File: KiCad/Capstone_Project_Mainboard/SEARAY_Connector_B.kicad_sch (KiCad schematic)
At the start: 1 part, among them J1 ASP-134486

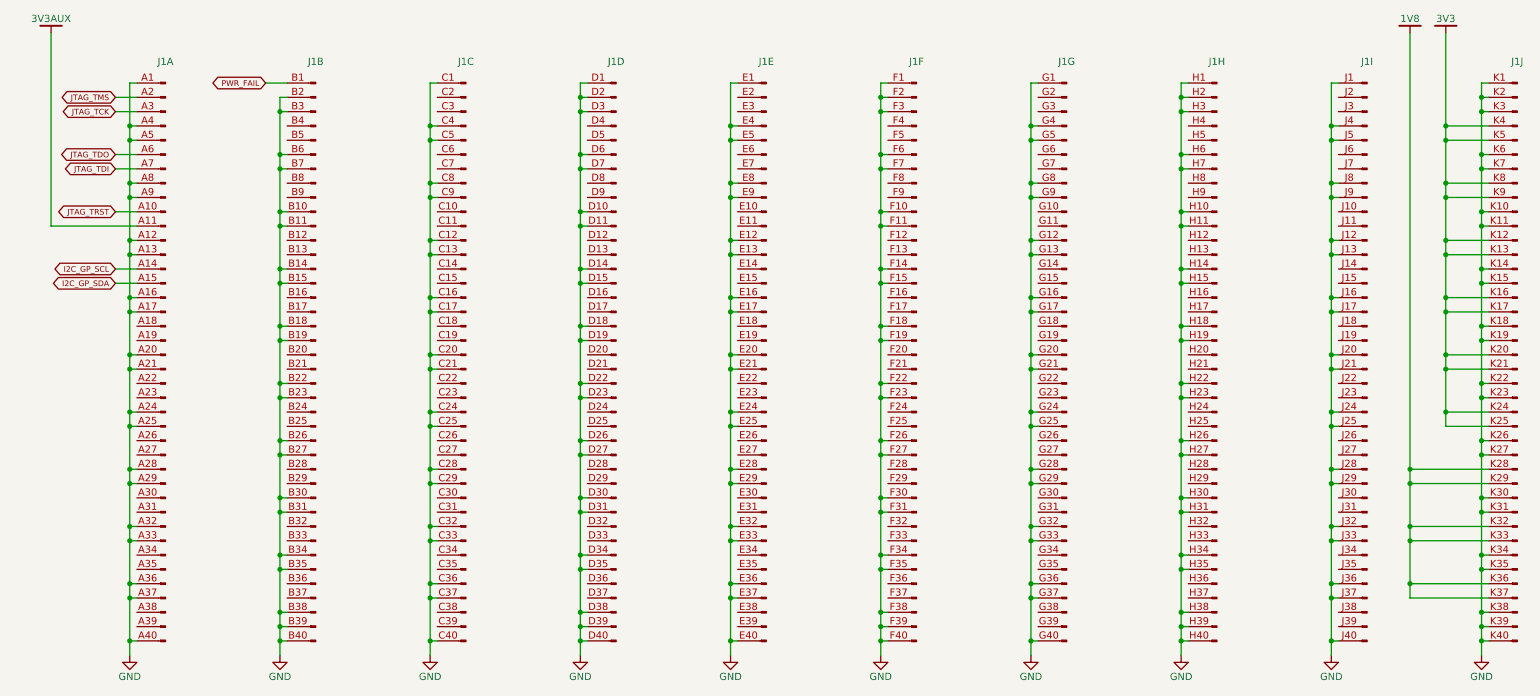
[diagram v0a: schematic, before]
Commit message: Updated FPGA Footprint
Added die-to-pad length offsets to all pins of the FFG676 package. These values were derived from the delay files provided in Vivado.
+ Other minor bugfixes
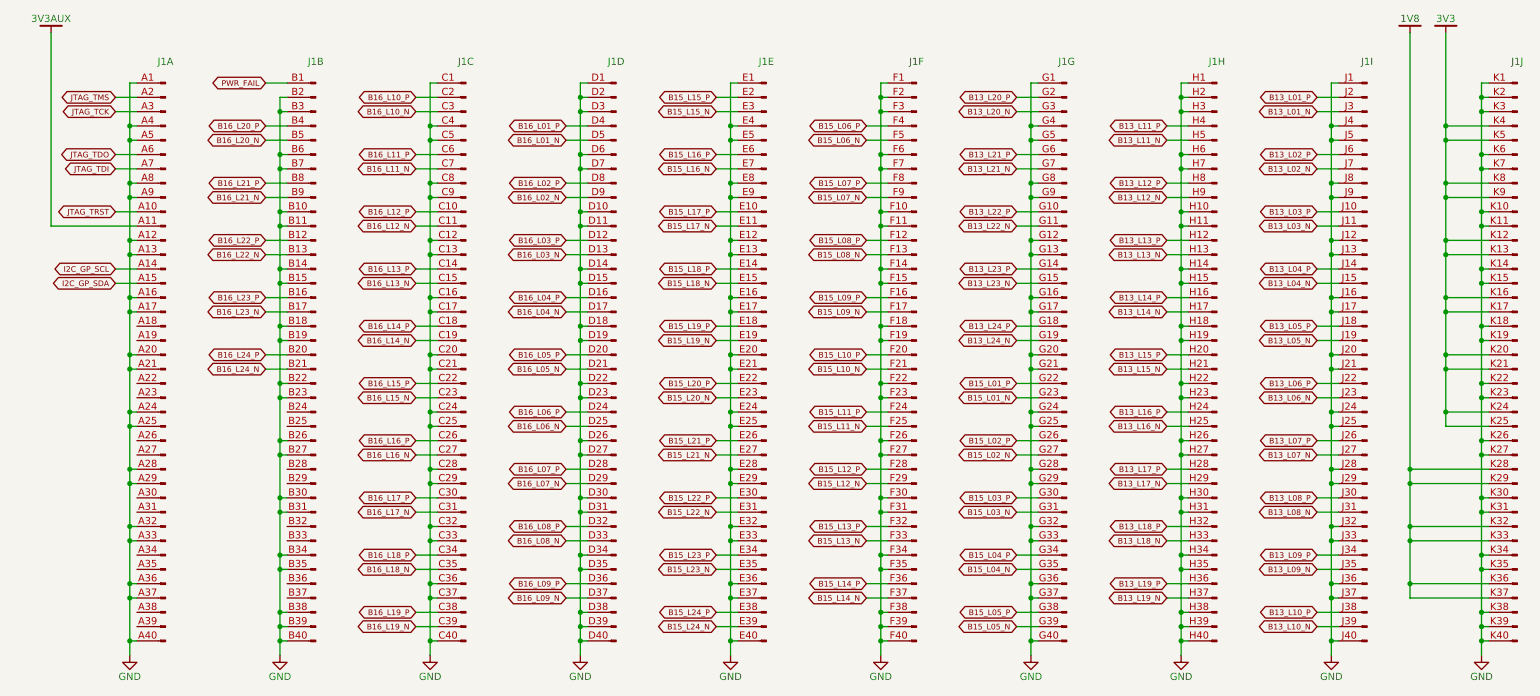
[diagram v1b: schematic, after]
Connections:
- net B16_L12_P: now reaches J1.C10 (Pin_10)
- net B16_L12_N: now reaches J1.C11 (Pin_11)
- net B16_L13_P: now reaches J1.C14 (Pin_14)
- net B16_L13_N: now reaches J1.C15 (Pin_15)
- net B16_L14_P: now reaches J1.C18 (Pin_18)
- net B16_L14_N: now reaches J1.C19 (Pin_19)
- net B16_L10_P: now reaches J1.C2 (Pin_2)
- net B16_L15_P: now reaches J1.C22 (Pin_22)
- net B16_L15_N: now reaches J1.C23 (Pin_23)
- net B16_L16_P: now reaches J1.C26 (Pin_26)
- net B16_L16_N: now reaches J1.C27 (Pin_27)
- net B16_L10_N: now reaches J1.C3 (Pin_3)
- net B16_L17_P: now reaches J1.C30 (Pin_30)
- net B16_L17_N: now reaches J1.C31 (Pin_31)
- net B16_L18_P: now reaches J1.C34 (Pin_34)
- net B16_L18_N: now reaches J1.C35 (Pin_35)
- net B16_L19_P: now reaches J1.C38 (Pin_38)
- net B16_L19_N: now reaches J1.C39 (Pin_39)
- net B16_L11_P: now reaches J1.C6 (Pin_6)
- net B16_L11_N: now reaches J1.C7 (Pin_7)
- net B15_L08_P: now reaches J1.F12 (Pin_12)
- net B15_L08_N: now reaches J1.F13 (Pin_13)
- net B15_L09_P: now reaches J1.F16 (Pin_16)
- net B15_L09_N: now reaches J1.F17 (Pin_17)
- net B15_L10_P: now reaches J1.F20 (Pin_20)
- net B15_L10_N: now reaches J1.F21 (Pin_21)
- net B15_L11_P: now reaches J1.F24 (Pin_24)
- net B15_L11_N: now reaches J1.F25 (Pin_25)
- net B15_L12_P: now reaches J1.F28 (Pin_28)
- net B15_L12_N: now reaches J1.F29 (Pin_29)
- net B15_L13_P: now reaches J1.F32 (Pin_32)
- net B15_L13_N: now reaches J1.F33 (Pin_33)
- net B15_L14_P: now reaches J1.F36 (Pin_36)
- net B15_L14_N: now reaches J1.F37 (Pin_37)
- net B15_L06_P: now reaches J1.F4 (Pin_4)
- net B15_L06_N: now reaches J1.F5 (Pin_5)
- net B15_L07_P: now reaches J1.F8 (Pin_8)
- net B15_L07_N: now reaches J1.F9 (Pin_9)
- net B16_L22_P: now reaches J1.B12 (Pin_12)
- net B16_L22_N: now reaches J1.B13 (Pin_13)
- net B16_L23_P: now reaches J1.B16 (Pin_16)
- net B16_L23_N: now reaches J1.B17 (Pin_17)
- net B16_L24_P: now reaches J1.B20 (Pin_20)
- net B16_L24_N: now reaches J1.B21 (Pin_21)
- net B16_L20_P: now reaches J1.B4 (Pin_4)
- net B16_L20_N: now reaches J1.B5 (Pin_5)
- net B16_L21_P: now reaches J1.B8 (Pin_8)
- net B16_L21_N: now reaches J1.B9 (Pin_9)
- net B13_L03_P: now reaches J1.J10 (Pin_10)
- net B13_L03_N: now reaches J1.J11 (Pin_11)
- net B13_L04_P: now reaches J1.J14 (Pin_14)
- net B13_L04_N: now reaches J1.J15 (Pin_15)
- net B13_L05_P: now reaches J1.J18 (Pin_18)
- net B13_L05_N: now reaches J1.J19 (Pin_19)
- net B13_L01_P: now reaches J1.J2 (Pin_2)
- net B13_L06_P: now reaches J1.J22 (Pin_22)
- net B13_L06_N: now reaches J1.J23 (Pin_23)
- net B13_L07_P: now reaches J1.J26 (Pin_26)
- net B13_L07_N: now reaches J1.J27 (Pin_27)
- net B13_L01_N: now reaches J1.J3 (Pin_3)
- net B13_L08_P: now reaches J1.J30 (Pin_30)
- net B13_L08_N: now reaches J1.J31 (Pin_31)
- net B13_L09_P: now reaches J1.J34 (Pin_34)
- net B13_L09_N: now reaches J1.J35 (Pin_35)
- net B13_L10_P: now reaches J1.J38 (Pin_38)
- net B13_L10_N: now reaches J1.J39 (Pin_39)
- net B13_L02_P: now reaches J1.J6 (Pin_6)
- net B13_L02_N: now reaches J1.J7 (Pin_7)
- net B13_L13_P: now reaches J1.H12 (Pin_12)
- net B13_L13_N: now reaches J1.H13 (Pin_13)
- net B13_L14_P: now reaches J1.H16 (Pin_16)
- net B13_L14_N: now reaches J1.H17 (Pin_17)
- net B13_L15_P: now reaches J1.H20 (Pin_20)
- net B13_L15_N: now reaches J1.H21 (Pin_21)
- net B13_L16_P: now reaches J1.H24 (Pin_24)
- net B13_L16_N: now reaches J1.H25 (Pin_25)
- net B13_L17_P: now reaches J1.H28 (Pin_28)
- net B13_L17_N: now reaches J1.H29 (Pin_29)
- net B13_L18_P: now reaches J1.H32 (Pin_32)
- net B13_L18_N: now reaches J1.H33 (Pin_33)
- net B13_L19_P: now reaches J1.H36 (Pin_36)
- net B13_L19_N: now reaches J1.H37 (Pin_37)
- net B13_L11_P: now reaches J1.H4 (Pin_4)
- net B13_L11_N: now reaches J1.H5 (Pin_5)
- net B13_L12_P: now reaches J1.H8 (Pin_8)
- net B13_L12_N: now reaches J1.H9 (Pin_9)
- net B15_L17_P: now reaches J1.E10 (Pin_10)
- net B15_L17_N: now reaches J1.E11 (Pin_11)
- net B15_L18_P: now reaches J1.E14 (Pin_14)
- net B15_L18_N: now reaches J1.E15 (Pin_15)
- net B15_L19_P: now reaches J1.E18 (Pin_18)
- net B15_L19_N: now reaches J1.E19 (Pin_19)
- net B15_L15_P: now reaches J1.E2 (Pin_2)
- net B15_L20_P: now reaches J1.E22 (Pin_22)
- net B15_L20_N: now reaches J1.E23 (Pin_23)
- net B15_L21_P: now reaches J1.E26 (Pin_26)
- net B15_L21_N: now reaches J1.E27 (Pin_27)
- net B15_L15_N: now reaches J1.E3 (Pin_3)
- net B15_L22_P: now reaches J1.E30 (Pin_30)
- net B15_L22_N: now reaches J1.E31 (Pin_31)
- net B15_L23_P: now reaches J1.E34 (Pin_34)
- net B15_L23_N: now reaches J1.E35 (Pin_35)
- net B15_L24_P: now reaches J1.E38 (Pin_38)
- net B15_L24_N: now reaches J1.E39 (Pin_39)
- net B15_L16_P: now reaches J1.E6 (Pin_6)
- net B15_L16_N: now reaches J1.E7 (Pin_7)
- net B16_L03_P: now reaches J1.D12 (Pin_12)
- net B16_L03_N: now reaches J1.D13 (Pin_13)
- net B16_L04_P: now reaches J1.D16 (Pin_16)
- net B16_L04_N: now reaches J1.D17 (Pin_17)
- net B16_L05_P: now reaches J1.D20 (Pin_20)
- net B16_L05_N: now reaches J1.D21 (Pin_21)
- net B16_L06_P: now reaches J1.D24 (Pin_24)
- net B16_L06_N: now reaches J1.D25 (Pin_25)
- net B16_L07_P: now reaches J1.D28 (Pin_28)
- net B16_L07_N: now reaches J1.D29 (Pin_29)
- net B16_L08_P: now reaches J1.D32 (Pin_32)
- net B16_L08_N: now reaches J1.D33 (Pin_33)
- net B16_L09_P: now reaches J1.D36 (Pin_36)
- net B16_L09_N: now reaches J1.D37 (Pin_37)
- net B16_L01_P: now reaches J1.D4 (Pin_4)
- net B16_L01_N: now reaches J1.D5 (Pin_5)
- net B16_L02_P: now reaches J1.D8 (Pin_8)
- net B16_L02_N: now reaches J1.D9 (Pin_9)
- net B13_L22_P: now reaches J1.G10 (Pin_10)
- net B13_L22_N: now reaches J1.G11 (Pin_11)
- net B13_L23_P: now reaches J1.G14 (Pin_14)
- net B13_L23_N: now reaches J1.G15 (Pin_15)
- net B13_L24_P: now reaches J1.G18 (Pin_18)
- net B13_L24_N: now reaches J1.G19 (Pin_19)
- net B13_L20_P: now reaches J1.G2 (Pin_2)
- net B15_L01_P: now reaches J1.G22 (Pin_22)
- net B15_L01_N: now reaches J1.G23 (Pin_23)
- net B15_L02_P: now reaches J1.G26 (Pin_26)
- net B15_L02_N: now reaches J1.G27 (Pin_27)
- net B13_L20_N: now reaches J1.G3 (Pin_3)
- net B15_L03_P: now reaches J1.G30 (Pin_30)
- net B15_L03_N: now reaches J1.G31 (Pin_31)
- net B15_L04_P: now reaches J1.G34 (Pin_34)
- net B15_L04_N: now reaches J1.G35 (Pin_35)
- net B15_L05_P: now reaches J1.G38 (Pin_38)
- net B15_L05_N: now reaches J1.G39 (Pin_39)
- net B13_L21_P: now reaches J1.G6 (Pin_6)
- net B13_L21_N: now reaches J1.G7 (Pin_7)

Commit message: Core non-power parts defined
Most major non-power components added to KiCad project
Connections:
- net I2C_GP_SCL renamed SEARAY_B_I2C_SCL
- net I2C_GP_SDA renamed SEARAY_B_I2C_SDA
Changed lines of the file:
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@@
   (title_block
     (title "10x40 SEARAY Connector B")
-    (date "2023-12-22")
+    (date "2023-12-26")
     (rev "A")
     (company "Jordan Harris-Toovy")
@@
     )
   )
-  (global_label "I2C_GP_SDA" (shape bidirectional) (at 33.02 72.39 180) (fields_autoplaced)
-    (effects (font (size 1 1) (color 65 65 65 1)) (justify right))
-    (property "Intersheetrefs" "${INTERSHEET_REFS}" (at 33.02 72.39 0)
-      (effects (font (size 1.27 1.27)) hide)
-    )
-  )
   (global_label "B15_L14_P" (shape bidirectional) (at 166.37 125.73 180) (fields_autoplaced)
     (effects (font (size 1 1) (color 65 65 65 1)) (justify right))
@@
     )
   )
-  (global_label "I2C_GP_SCL" (shape bidirectional) (at 33.02 69.85 180) (fields_autoplaced)
-    (effects (font (size 1 1) (color 65 65 65 1)) (justify right))
-    (property "Intersheetrefs" "${INTERSHEET_REFS}" (at 33.02 69.85 0)
-      (effects (font (size 1.27 1.27)) hide)
-    )
-  )
   (global_label "B15_L09_N" (shape bidirectional) (at 166.37 77.47 180) (fields_autoplaced)
     (effects (font (size 1 1) (color 65 65 65 1)) (justify right))
@@
     )
   )
+  (global_label "SEARAY_B_I2C_SDA" (shape bidirectional) (at 33.02 72.39 180) (fields_autoplaced)
+    (effects (font (size 1 1) (color 65 65 65 1)) (justify right))
+    (property "Intersheetrefs" "${INTERSHEET_REFS}" (at 15.8424 72.39 0)
+      (effects (font (size 1.27 1.27)) (justify right) hide)
+    )
+  )
   (global_label "B13_L12_N" (shape bidirectional) (at 219.71 57.15 180) (fields_autoplaced)
     (effects (font (size 1 1) (color 65 65 65 1)) (justify right))
@@
     )
   )
+  (global_label "SEARAY_B_I2C_SCL" (shape bidirectional) (at 33.02 69.85 180) (fields_autoplaced)
+    (effects (font (size 1 1) (color 65 65 65 1)) (justify right))
+    (property "Intersheetrefs" "${INTERSHEET_REFS}" (at 15.89 69.85 0)
+      (effects (font (size 1.27 1.27)) (justify right) hide)
+    )
+  )
